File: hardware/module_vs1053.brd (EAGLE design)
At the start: 109.9 x 68.6 mm, 119 parts, among them IC1 IC_USBLC6-2, IC2 LM1117IMPX-3.3, IC3 PIC32MX795F512, IC4 DP83848, IC5 LM1117MPX-2.5, U1 USD-SOCKETUSD, U3 VS1053-L, X2 CRYSTALS-NOGND-CFPX-217, X3 KUSBVX, Y3 CRYSTAL-GROUNDEDSMD-5X3.2

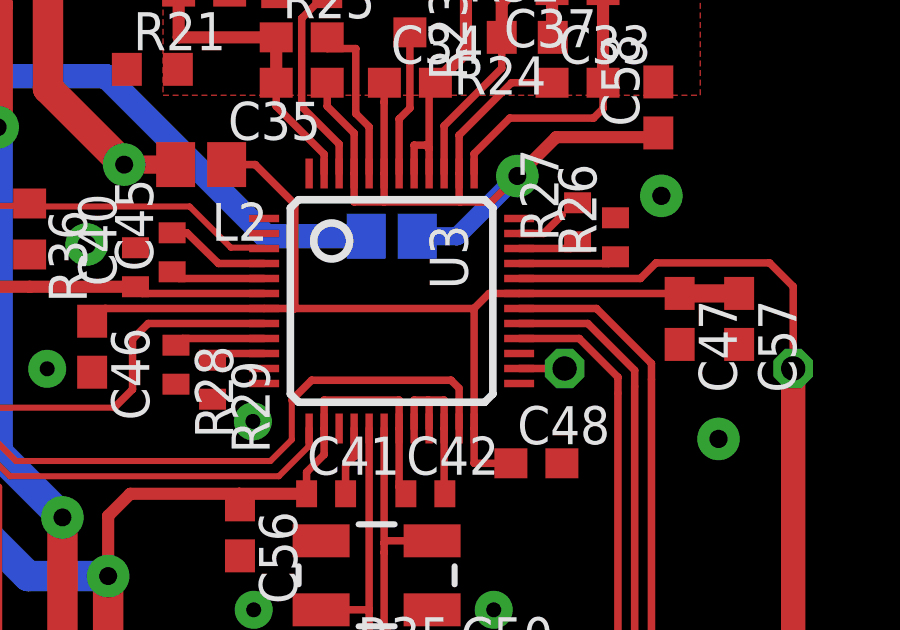
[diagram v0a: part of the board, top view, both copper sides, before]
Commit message: VS1053 version updated
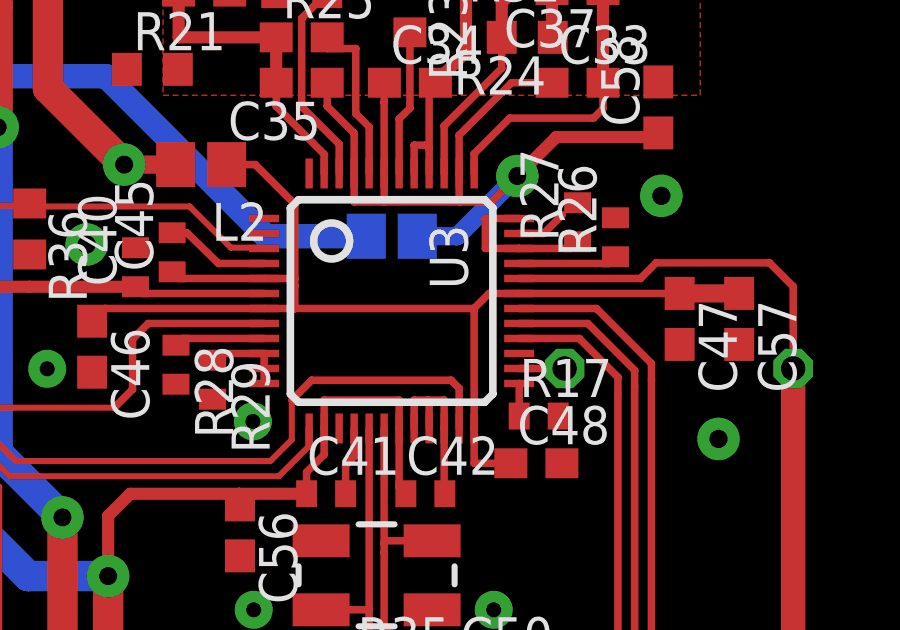
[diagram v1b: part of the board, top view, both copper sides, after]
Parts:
- added R17: 100k, rcl:R0402
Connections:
- new net N$2: R17.1, U3.25
- net GND: now also R17.2
- net VS_N$26: now also U3.11, U3.12
- net VS_N$28: now also U3.36
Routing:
- net VS_N$28: track 2.04 -> 5.29 mm
- net N$2: track 0.00 -> 1.09 mm
- net VS_CVDD: track 37.8 -> 38.8 mm
- net VS_N$26: track 1.81 -> 2.81 mm
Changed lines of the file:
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@@
 <element name="R16" library="rcl" package="R0603" value="" x="20.574" y="10.6544" rot="MR270"/>
 <element name="U3" library="vlsi-web" package="LQFP48" value="VS1053-L" x="91.44" y="42.672" rot="R270"/>
+<element name="R17" library="rcl" package="R0402" value="100k" x="96.3422" y="38.8366"/>
 </elements>
 <signals>
@@
 <wire x1="95.69" y1="44.922" x2="96.5094" y2="44.922" width="0.251459375" layer="1"/>
 <wire x1="96.5094" y1="44.922" x2="97.1296" y2="45.5422" width="0.251459375" layer="1"/>
+<contactref element="R17" pad="2"/>
 </signal>
 <signal name="A3V">
@@
 <contactref element="C47" pad="1"/>
 <contactref element="C45" pad="1"/>
-<wire x1="88.2142" y1="42.418" x2="88.2142" y2="45.8978" width="0.251459375" layer="1"/>
+<wire x1="88.2142" y1="42.418" x2="88.2142" y2="43.18" width="0.251459375" layer="1"/>
+<wire x1="88.2142" y1="43.422" x2="88.2142" y2="45.8978" width="0.251459375" layer="1"/>
 <wire x1="94.186" y1="42.422" x2="94.19" y2="42.418" width="0.251459375" layer="1"/>
 <wire x1="94.19" y1="42.426" x2="94.186" y2="42.422" width="0.251459375" layer="1"/>
@@
 <wire x1="94.19" y1="42.426" x2="94.686" y2="42.922" width="0.251459375" layer="1"/>
 <wire x1="94.19" y1="37.2618" x2="94.19" y2="38.422" width="0.251459375" layer="1"/>
-<wire x1="87.19" y1="42.422" x2="87.19" y2="43.422" width="0" layer="19" extent="1-1"/>
+<wire x1="87.19" y1="43.422" x2="88.2142" y2="43.422" width="0.251459375" layer="1"/>
+<wire x1="88.2142" y1="43.422" x2="88.2142" y2="43.18" width="0.251459375" layer="1"/>
 </signal>
 <signal name="_1V8">
@@
 <wire x1="87.19" y1="40.922" x2="85.69481875" y2="40.922" width="0.251459375" layer="1"/>
 <wire x1="85.69481875" y1="40.922" x2="85.471" y2="40.69818125" width="0.251459375" layer="1"/>
+<contactref element="U3" pad="11"/>
+<contactref element="U3" pad="12"/>
+<wire x1="87.19" y1="39.922" x2="87.19" y2="40.422" width="0.251459375" layer="1"/>
+<wire x1="87.19" y1="40.422" x2="87.19" y2="40.922" width="0.251459375" layer="1"/>
 </signal>
 <signal name="VS_N$27">
@@
 <wire x1="95.69" y1="44.422" x2="97.41378125" y2="44.422" width="0.251459375" layer="1"/>
 <wire x1="97.41378125" y1="44.422" x2="97.6376" y2="44.64581875" width="0.251459375" layer="1"/>
+<contactref element="U3" pad="36"/>
+<wire x1="95.69" y1="45.422" x2="94.5642" y2="45.422" width="0.251459375" layer="1"/>
+<wire x1="94.5642" y1="45.422" x2="94.5642" y2="44.4246" width="0.251459375" layer="1"/>
+<wire x1="94.5642" y1="44.4246" x2="95.69" y2="44.4246" width="0.251459375" layer="1"/>
+<wire x1="95.69" y1="44.4246" x2="95.69" y2="44.422" width="0.251459375" layer="1"/>
 </signal>
 <signal name="VS_N$30">
@@
 <contactref element="IC3" pad="67"/>
 </signal>
+<signal name="N$2">
+<contactref element="U3" pad="25"/>
+<contactref element="R17" pad="1"/>
+<wire x1="95.69" y1="39.922" x2="95.6922" y2="39.922" width="0.251459375" layer="1"/>
+<wire x1="95.6922" y1="39.922" x2="95.6922" y2="38.8366" width="0.251459375" layer="1"/>
+</signal>
 </signals>

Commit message: PCB updated
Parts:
- removed JP1: (no value), SparkFun-Connectors:AUDIO-JACK2
- added J1: AUDIO_JACK_TRRSSMD_RA, SparkFun-Connectors:AUDIO_JACK_3.5MM_TRRS_SMD_RA
- moved C33 2.54 mm to (97.6, 47.4)
- moved C34 2.54 mm to (92.0, 47.4)
- moved C35 2.54 mm to (88.4, 47.4)
- moved C37 2.54 mm to (97.6, 50.5)
- moved C46 2.54 mm to (81.5, 38.6)
- moved C58 2.54 mm to (100.3, 46.6)
- moved L1 2.54 mm to (91.4, 42.3)
- moved R28 2.54 mm to (84.3, 38.0)
- moved C36 2.54 mm to (92.0, 54.2)
- moved C39 2.54 mm to (85.2, 50.4)
- moved C40 2.54 mm to (82.9, 41.3)
- moved C41 2.54 mm to (89.3, 33.7)
- moved C42 2.54 mm to (92.6, 33.7)
- moved C43 2.54 mm to (88.4, 53.6)
- moved C44 2.54 mm to (96.4, 53.6)
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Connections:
- net VS_AGND: now also J1.EARTH; no longer JP1.SLEEVE
- net VS_N$37: now also J1.RING1; no longer JP1.RING
- net VS_N$38: now also J1.TIP; no longer JP1.TIP
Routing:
- net VS_AGND: track 78.1 -> 54.1 mm
- net VS_N$37: track 5.51 -> 11.6 mm
- net VS_N$38: track 4.42 -> 7.17 mm
- net _1V8: track 27.6 -> 30.3 mm, vias 1 -> 0
- net VS_MOSI: track 69.1 -> 71.3 mm
- net VS_SCK: track 71.6 -> 69.5 mm
- net VS_MISO: track 90.8 -> 92.0 mm
- net VBUS: track 191.0 -> 189.9 mm
- net VS_XRST: track 40.9 -> 41.9 mm
- net VS_XDCS: track 43.4 -> 44.5 mm
- net VS_DREQ: track 44.1 -> 45.2 mm
- net VS_XCS: track 51.6 -> 52.6 mm
- net 3V: track 542.6 -> 542.1 mm

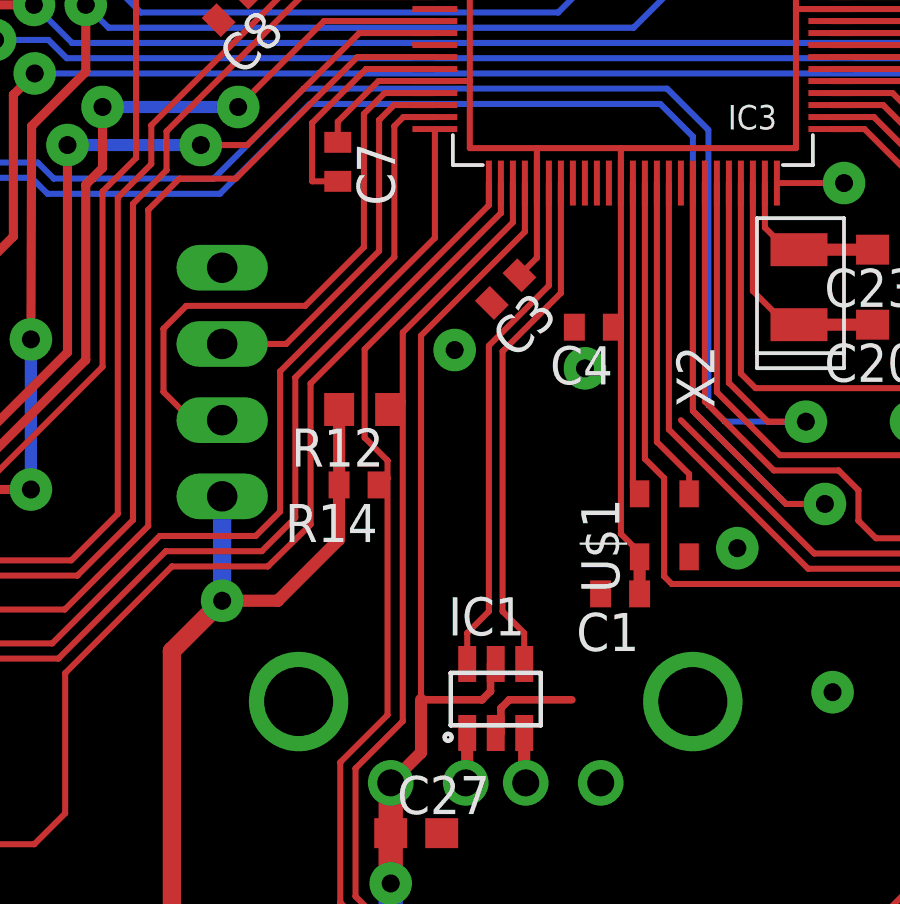
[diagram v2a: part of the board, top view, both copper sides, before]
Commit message: Changes in PCB design allowing us to use bug free I2C1 instead of buggy I2C3
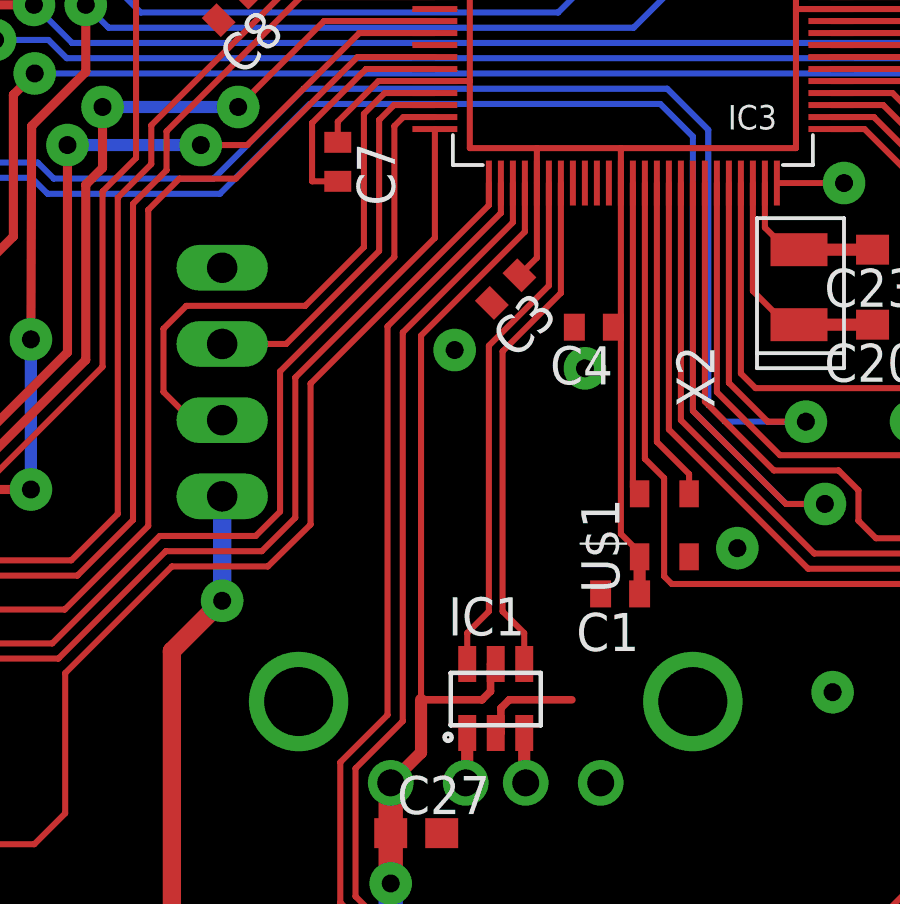
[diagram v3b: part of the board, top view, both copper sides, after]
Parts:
- removed R12: (no value), rcl:R0603
- removed R14: (no value), rcl:R0402
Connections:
- net 1WIRE renamed SCL1
- removed net LED: SV1.6
- removed net RA15_ROT_SW: IC3.67
- removed net SCL1A: IC3.53, R12.1, SV1.1
- removed net SDA1A: IC3.52, R14.1, SV1.2
- new net RF2: IC3.52, SV1.2
- new net RF8: IC3.53, SV1.1
- new net SDA1: IC3.67, SV1.6
- net 3V: no longer R12.2, R14.2
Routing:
- net SCL1A: track 49.0 -> 0.00 mm
- net SDA1A: track 48.4 -> 0.00 mm
- net RF8: track 0.00 -> 48.4 mm
- net RF2: track 0.00 -> 47.4 mm
- net SDA1: track 0.00 -> 31.6 mm
- net LED: track 23.7 -> 0.00 mm
- net 3V: track 542.1 -> 533.0 mm
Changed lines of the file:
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@@
 </element>
 <element name="C1" library="rcl" package="C0402" value="" x="49.86601875" y="18.9992" rot="R180"/>
-<element name="R12" library="rcl" package="R0603" value="" x="41.3512" y="25.146" rot="R180"/>
-<element name="R14" library="rcl" package="R0402" value="" x="41.148" y="22.6314" rot="R180"/>
 <element name="C2" library="rcl" package="C0402" value="" x="26.126440625" y="25.5016"/>
 <element name="L3" library="dp_devices" package="FB805" value="" x="11.938" y="38.4302" rot="MR180"/>
@@
 <wire x1="43.692" y1="39.6938" x2="38.0555" y2="39.6938" width="0.2032" layer="1"/>
 <wire x1="38.0555" y1="39.6938" x2="37.40391875" y2="39.04221875" width="0.2032" layer="1"/>
-<contactref element="R12" pad="2"/>
-<contactref element="R14" pad="2"/>
-<wire x1="40.5012" y1="25.146" x2="40.5012" y2="22.6346" width="0.4064" layer="1"/>
-<wire x1="40.5012" y1="22.6346" x2="40.498" y2="22.6314" width="0.4064" layer="1"/>
-<wire x1="40.498" y1="22.6314" x2="40.498" y2="20.813" width="0.4064" layer="1"/>
-<wire x1="36.6014" y1="18.7706" x2="38.4556" y2="18.7706" width="0.4064" layer="1"/>
-<wire x1="38.4556" y1="18.7706" x2="40.498" y2="20.813" width="0.4064" layer="1"/>
 <wire x1="36.6014" y1="18.7706" x2="36.6014" y2="22.2504" width="0.6096" layer="16"/>
 <wire x1="36.6014" y1="18.7706" x2="34.925" y2="17.0942" width="0.6096" layer="1"/>
@@
 <wire x1="63.373" y1="14.351" x2="65.659" y2="12.065" width="0.2032" layer="1"/>
 </signal>
-<signal name="LED">
-<wire x1="51.892" y1="24.7906" x2="56.3372" y2="20.3454" width="0.2032" layer="1"/>
-<contactref element="SV1" pad="6"/>
-<wire x1="56.3372" y1="20.3454" x2="61.0362" y2="20.3454" width="0.2032" layer="1"/>
-<wire x1="61.0362" y1="20.3454" x2="62.865" y2="18.5166" width="0.2032" layer="1"/>
-<wire x1="62.865" y1="18.5166" x2="62.865" y2="14.1224" width="0.2032" layer="1"/>
-<wire x1="62.865" y1="14.1224" x2="64.389" y2="12.5984" width="0.2032" layer="1"/>
-<wire x1="64.389" y1="12.5984" x2="64.389" y2="10.795" width="0.2032" layer="1"/>
-<wire x1="64.389" y1="10.795" x2="65.659" y2="9.525" width="0.2032" layer="1"/>
-</signal>
-<signal name="1WIRE">
+<signal name="SCL1">
 <contactref element="IC3" pad="66"/>
 <wire x1="51.492" y1="32.6938" x2="51.492" y2="24.4794" width="0.2032" layer="1"/>
@@
 <wire x1="28.702" y1="63.0682" x2="30.2768" y2="64.643" width="0.4064" layer="1"/>
 </signal>
-<signal name="SCL1A">
+<signal name="RF8">
 <contactref element="IC3" pad="53"/>
 <wire x1="46.292" y1="32.6938" x2="46.292" y2="31.3822" width="0.2032" layer="1"/>
@@
 <wire x1="59.3344" y1="8.9916" x2="59.3344" y2="10.8204" width="0.2032" layer="1"/>
 <wire x1="59.3344" y1="10.8204" x2="60.579" y2="12.065" width="0.2032" layer="1"/>
-<contactref element="R12" pad="1"/>
-<wire x1="42.6212" y1="27.7114" x2="42.6212" y2="25.4" width="0.2032" layer="1"/>
-<wire x1="42.6212" y1="25.4" x2="42.6212" y2="14.7574" width="0.2032" layer="1"/>
-<wire x1="42.2012" y1="25.146" x2="42.3672" y2="25.146" width="0.2032" layer="1"/>
-<wire x1="42.3672" y1="25.146" x2="42.6212" y2="25.4" width="0.2032" layer="1"/>
+<wire x1="42.6212" y1="27.7114" x2="42.6212" y2="14.7574" width="0.2032" layer="1"/>
 </signal>
 <signal name="DP_RST">
@@
 <wire x1="61.849" y1="10.795" x2="63.119" y2="9.525" width="0.2032" layer="1"/>
 </signal>
-<signal name="SDA1A">
+<signal name="RF2">
 <contactref element="IC3" pad="52"/>
 <wire x1="45.892" y1="32.6938" x2="45.892" y2="31.6934" width="0.2032" layer="1"/>
-<wire x1="45.892" y1="31.6934" x2="41.3512" y2="27.1526" width="0.2032" layer="1"/>
+<wire x1="45.892" y1="31.6934" x2="42.1132" y2="27.9146" width="0.2032" layer="1"/>
 <contactref element="SV1" pad="2"/>
 <wire x1="40.5384" y1="13.3858" x2="40.5384" y2="8.7122" width="0.2032" layer="1"/>
@@
 <wire x1="41.529" y1="7.7216" x2="58.7756" y2="7.7216" width="0.2032" layer="1"/>
 <wire x1="58.7756" y1="7.7216" x2="60.579" y2="9.525" width="0.2032" layer="1"/>
-<contactref element="R14" pad="1"/>
 <wire x1="42.1132" y1="14.9606" x2="40.5384" y2="13.3858" width="0.2032" layer="1"/>
-<wire x1="41.3512" y1="27.1526" x2="41.3512" y2="24.2062" width="0.2032" layer="1"/>
-<wire x1="42.1132" y1="23.4442" x2="42.1132" y2="22.86" width="0.2032" layer="1"/>
-<wire x1="42.1132" y1="22.86" x2="42.1132" y2="14.9606" width="0.2032" layer="1"/>
-<wire x1="41.798" y1="22.6314" x2="41.8846" y2="22.6314" width="0.2032" layer="1"/>
-<wire x1="41.8846" y1="22.6314" x2="42.1132" y2="22.86" width="0.2032" layer="1"/>
-<wire x1="41.3512" y1="24.2062" x2="42.1132" y2="23.4442" width="0.2032" layer="1"/>
-</signal>
-<signal name="RA15_ROT_SW">
+<wire x1="42.1132" y1="27.9146" x2="42.1132" y2="14.9606" width="0.2032" layer="1"/>
+</signal>
+<signal name="SDA1">
 <contactref element="IC3" pad="67"/>
+<wire x1="51.892" y1="24.7906" x2="56.3372" y2="20.3454" width="0.2032" layer="1"/>
+<contactref element="SV1" pad="6"/>
+<wire x1="56.3372" y1="20.3454" x2="61.0362" y2="20.3454" width="0.2032" layer="1"/>
+<wire x1="61.0362" y1="20.3454" x2="62.865" y2="18.5166" width="0.2032" layer="1"/>
+<wire x1="62.865" y1="18.5166" x2="62.865" y2="14.1224" width="0.2032" layer="1"/>
+<wire x1="62.865" y1="14.1224" x2="64.389" y2="12.5984" width="0.2032" layer="1"/>
+<wire x1="64.389" y1="12.5984" x2="64.389" y2="10.795" width="0.2032" layer="1"/>
+<wire x1="64.389" y1="10.795" x2="65.659" y2="9.525" width="0.2032" layer="1"/>
+<wire x1="51.892" y1="24.7906" x2="51.892" y2="32.6938" width="0.2032" layer="1"/>
 </signal>
 <signal name="N$2">

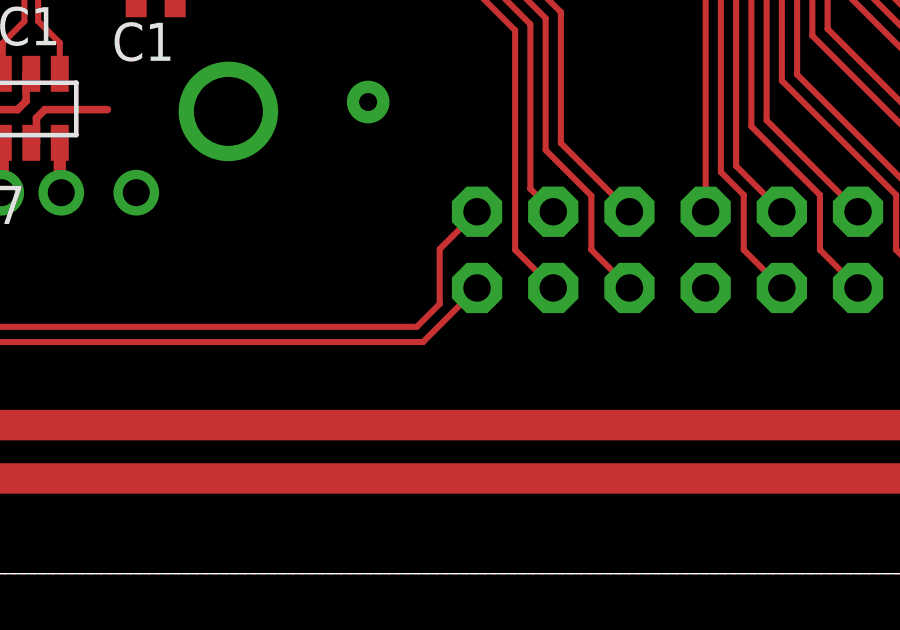
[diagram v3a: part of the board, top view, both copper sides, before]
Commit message: Changes to prepare project for analog radio funcionality
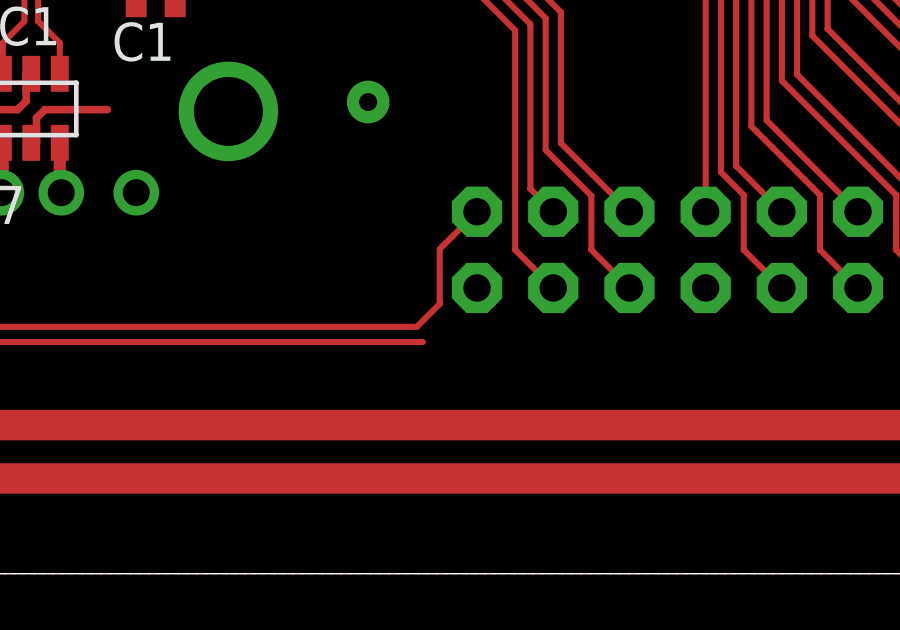
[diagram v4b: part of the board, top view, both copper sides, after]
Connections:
- new net RF2_ROT_SW: SV1.2
- net RF2: no longer SV1.2
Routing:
- net RF2: track 47.4 -> 44.8 mm
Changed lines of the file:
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@@
 <wire x1="45.892" y1="32.6938" x2="45.892" y2="31.6934" width="0.2032" layer="1"/>
 <wire x1="45.892" y1="31.6934" x2="42.1132" y2="27.9146" width="0.2032" layer="1"/>
-<contactref element="SV1" pad="2"/>
 <wire x1="40.5384" y1="13.3858" x2="40.5384" y2="8.7122" width="0.2032" layer="1"/>
 <wire x1="40.5384" y1="8.7122" x2="41.529" y2="7.7216" width="0.2032" layer="1"/>
 <wire x1="41.529" y1="7.7216" x2="58.7756" y2="7.7216" width="0.2032" layer="1"/>
-<wire x1="58.7756" y1="7.7216" x2="60.579" y2="9.525" width="0.2032" layer="1"/>
 <wire x1="42.1132" y1="14.9606" x2="40.5384" y2="13.3858" width="0.2032" layer="1"/>
 <wire x1="42.1132" y1="27.9146" x2="42.1132" y2="14.9606" width="0.2032" layer="1"/>
@@
 <wire x1="95.6922" y1="37.382" x2="95.6922" y2="36.2966" width="0.251459375" layer="1"/>
 </signal>
+<signal name="RF2_ROT_SW">
+<contactref element="SV1" pad="2"/>
+</signal>
 </signals>
